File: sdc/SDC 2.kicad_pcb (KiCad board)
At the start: 2 copper layers, 70 x 56 mm, 122 parts, among them J1 BSPD_LED, J10 BMS_LED, J11 BSPD_Fault, J12 IMD_Fault, J13 BMS_Fault, J14 12V PWR, J15 SDC_IN, J16 SDC_OUT, J2 IMD_LED, J3 BMS_LED, J4 SW_Fault, J5 BSPD_BTN, J6 IMD_BTN, J7 BMS_BTN, J8 BSPD_LED, J9 IMD_LED, K1 G2RL-2A, K2 G2RL-2A, K3 G2RL-2A, K4 G2RL-2A, Q1 2N7002, Q2 2N7002, Q3 2N7002, Q4 2N7002, Q5 2N7002, Q6 2N7002, U1 VOM618AT, U10 AP2204K-ADJ, U2 VOM618AT, U3 TLV2371DBV, U4 TLV2371DBV, U6 VOM618AT, U7 VOM618AT, U8 TLV2371DBV, U9 AP2204K-ADJ

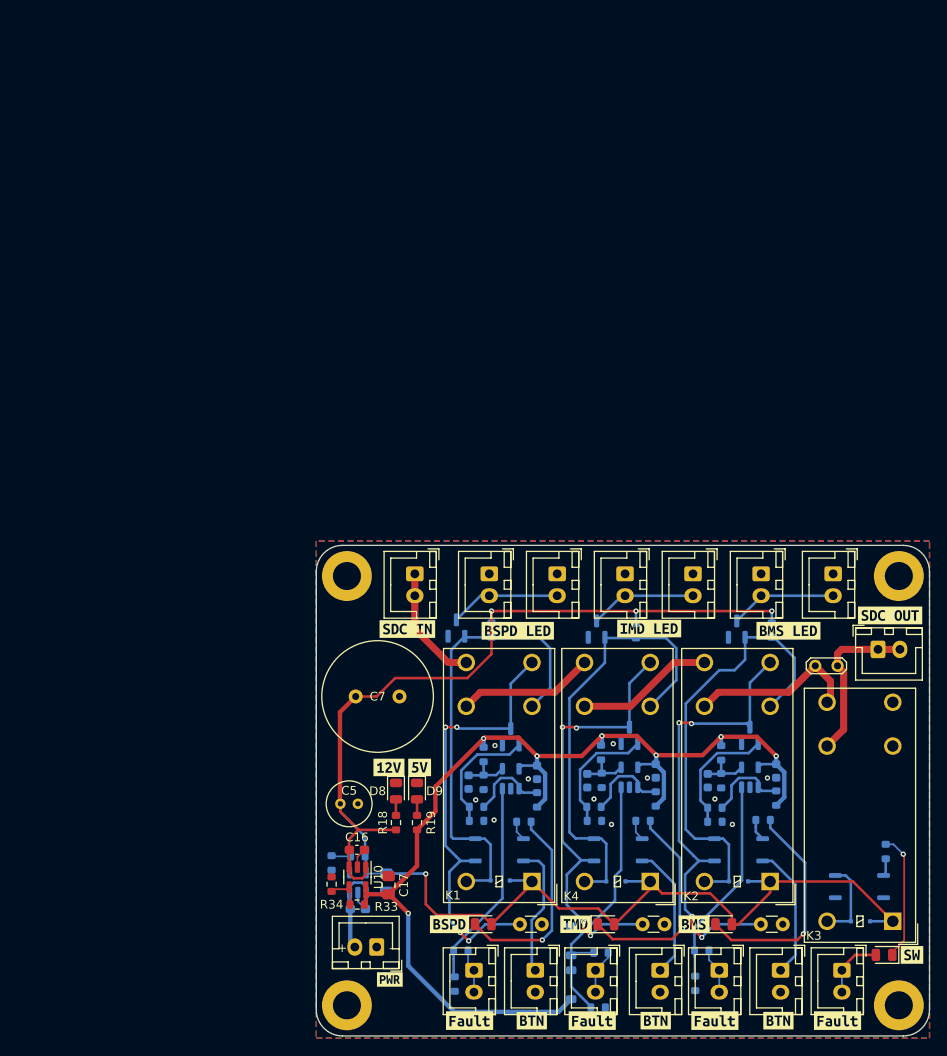
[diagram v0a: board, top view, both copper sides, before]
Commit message: Change JST to pin header
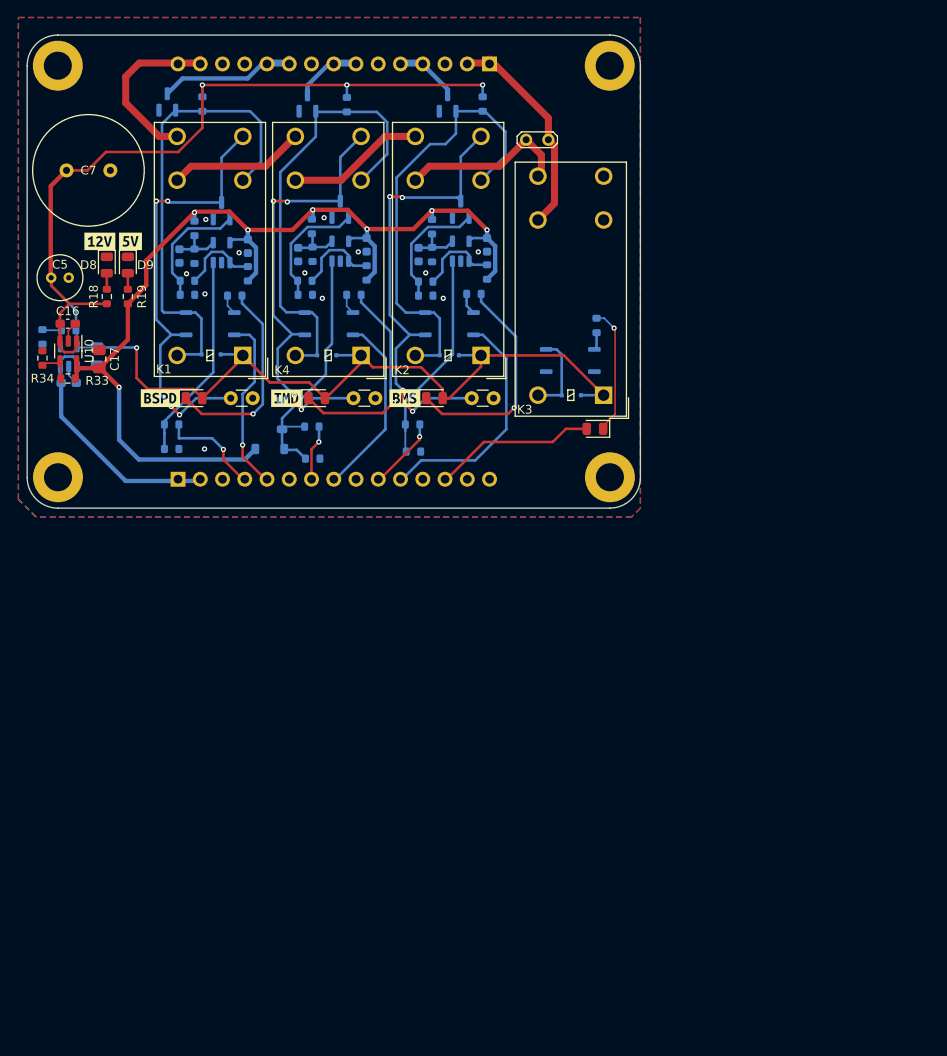
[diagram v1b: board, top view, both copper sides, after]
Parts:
- removed J1, J8: BSPD_LED, Connector_JST:JST_XH_B2B-XH-A_1x02_P2.50mm_Vertical
- removed J10, J3: BMS_LED, Connector_JST:JST_XH_B2B-XH-A_1x02_P2.50mm_Vertical
- removed J11: BSPD_Fault, Connector_JST:JST_XH_B2B-XH-A_1x02_P2.50mm_Vertical
- removed J12: IMD_Fault, Connector_JST:JST_XH_B2B-XH-A_1x02_P2.50mm_Vertical
- removed J13: BMS_Fault, Connector_JST:JST_XH_B2B-XH-A_1x02_P2.50mm_Vertical
- removed J14: 12V PWR, Connector_JST:JST_XH_B2B-XH-A_1x02_P2.50mm_Vertical
- removed J15: SDC_IN, Connector_JST:JST_XH_B2B-XH-A_1x02_P2.50mm_Vertical
- removed J16: SDC_OUT, Connector_JST:JST_XH_B2B-XH-A_1x02_P2.50mm_Vertical
- removed J2, J9: IMD_LED, Connector_JST:JST_XH_B2B-XH-A_1x02_P2.50mm_Vertical
- removed J4: SW_Fault, Connector_JST:JST_XH_B2B-XH-A_1x02_P2.50mm_Vertical
- removed J5: BSPD_BTN, Connector_JST:JST_XH_B2B-XH-A_1x02_P2.50mm_Vertical
- removed J6: IMD_BTN, Connector_JST:JST_XH_B2B-XH-A_1x02_P2.50mm_Vertical
- removed J7: BMS_BTN, Connector_JST:JST_XH_B2B-XH-A_1x02_P2.50mm_Vertical
- removed kibuzzard-67515B12: G***, kibuzzard-67515B12
- removed kibuzzard-67515B3D: G***, kibuzzard-67515B3D
- removed kibuzzard-67515B49: G***, kibuzzard-67515B49
- removed kibuzzard-67515B54: G***, kibuzzard-67515B54
- removed kibuzzard-67515B5C: G***, kibuzzard-67515B5C
- removed kibuzzard-67515BF5 (x3): G***, kibuzzard-67515BF5
- removed kibuzzard-67515BFB (x3): G***, kibuzzard-67515BFB
- removed kibuzzard-675169EE: G***, kibuzzard-675169EE
- removed kibuzzard-675169F2: G***, kibuzzard-675169F2
- removed kibuzzard-67A0C7EA: G***, kibuzzard-67A0C7EA
- added J17: Conn_01x15_Pin, Connector_PinHeader_2.54mm:PinHeader_1x15_P2.54mm_Vertical, B.Cu at (106.8, 49.3)
- added J18: Conn_01x15_Pin, Connector_PinHeader_2.54mm:PinHeader_1x15_P2.54mm_Vertical, B.Cu at (71.2, 96.7)
- moved R22 70.6 mm to (86.6, 94.3)
- moved D6 70.2 mm to (81.7, 93.2), turned to 0 degrees
- moved R5 69.1 mm to (70.5, 93.2), turned to 0 degrees
- moved H2 68.7 mm to (57.5, 96.5)
- moved H4 68.7 mm to (120.5, 96.5)
- moved R6 68.7 mm to (98.1, 93.5), turned to 0 degrees
- moved R11 68.5 mm to (79.2, 73.2)
- moved R3 68.5 mm to (77.7, 75.8)
- moved R34 68.5 mm to (55.7, 82.9)
- moved U10 68.5 mm to (58.7, 82.1)
- moved C1 68.5 mm to (71.4, 71.2)
- moved C10 68.5 mm to (79.2, 70.1)
- moved C11 68.5 mm to (91.2, 87.5)
- moved C12 68.5 mm to (77.2, 87.5)
- moved C13 68.5 mm to (104.7, 87.5)
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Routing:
- net VDC: track 10.1 -> 28.3 mm
- net SW_Fault: track 6.18 -> 18.3 mm
- net BMS_RST: track 15.4 -> 27.5 mm
- net BSPD_FAULT: track 4.53 -> 11.8 mm, vias 0 -> 1
- net BSPD_IN: track 13.3 -> 19.8 mm
- net SW_OUT: track 18.5 -> 24.8 mm
- net IMD_RST: track 15.4 -> 21.3 mm
- net BSPD_RST: track 15.2 -> 20.4 mm, vias 0 -> 1
- net BMS_LED: track 12.2 -> 7.19 mm
- net IMD_LED: track 12.4 -> 7.85 mm
- net +5V: track 125.0 -> 120.6 mm
- net BSPD_LED: track 12.6 -> 16.5 mm
- net BMS_FAULT: track 4.74 -> 8.41 mm, vias 0 -> 1
- net IMD_FAULT: track 4.60 -> 6.56 mm, vias 0 -> 1
- net Net-(D6-A): track 31.6 -> 29.7 mm
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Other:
- board size 70 x 56 mm -> 70 x 54 mm
- board text removed: "+ -"

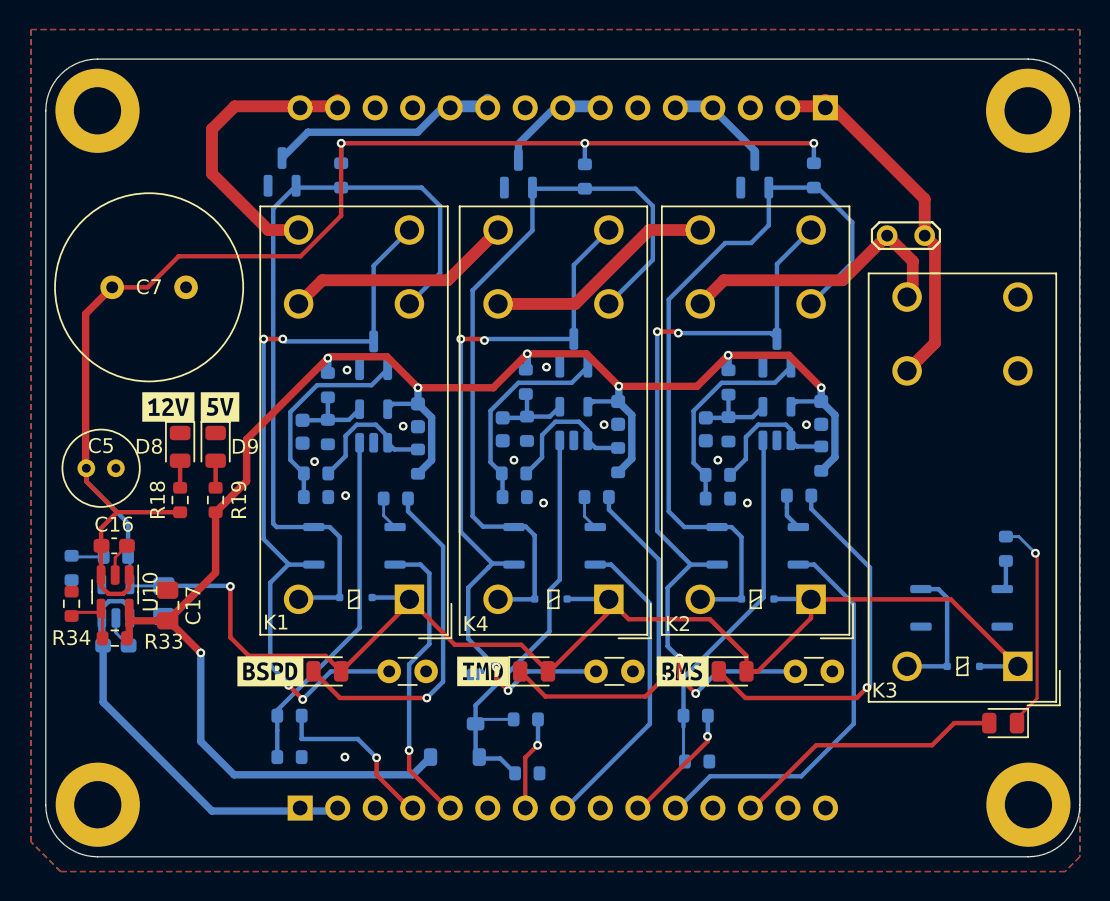
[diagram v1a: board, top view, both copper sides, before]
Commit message: feat: use 2x10 pin
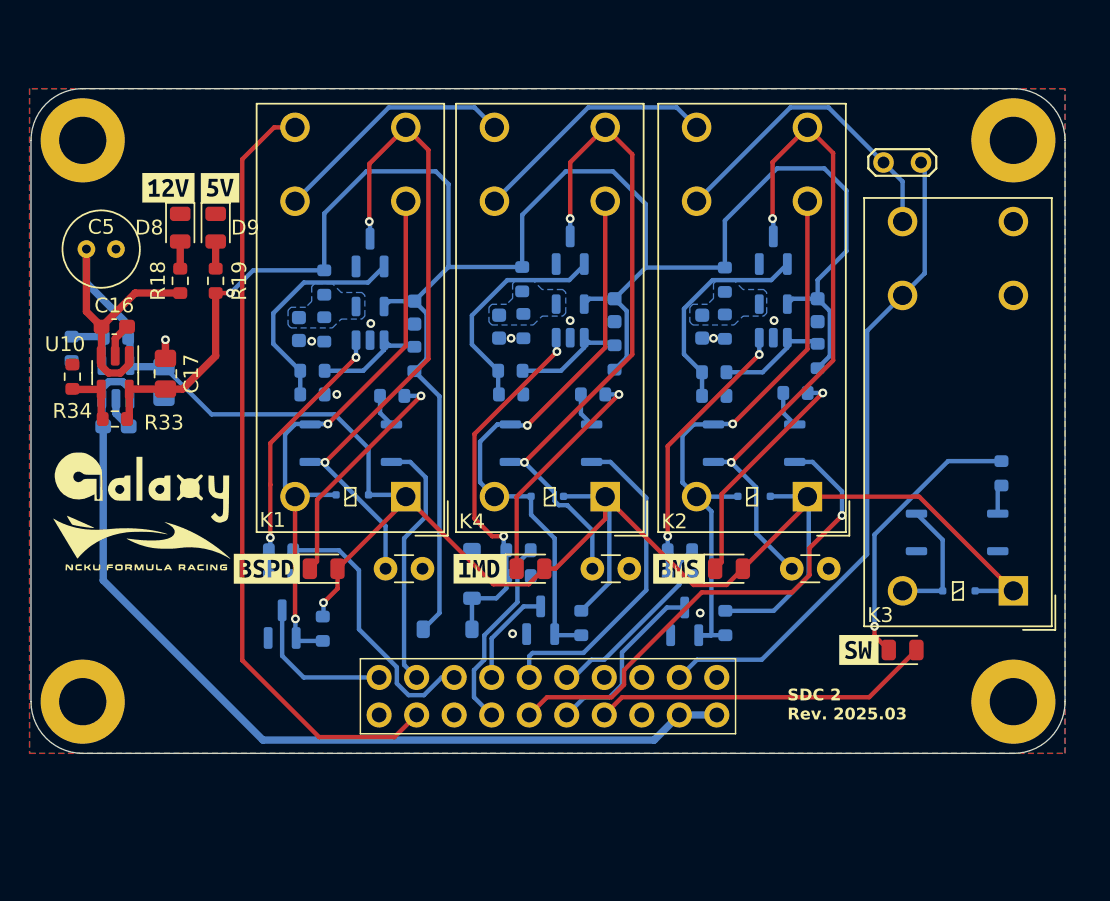
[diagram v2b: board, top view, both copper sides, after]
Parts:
- removed C7: 220u, Capacitor_THT:C_Radial_D12.5mm_H25.0mm_P5.00mm
- removed J17, J18: Conn_01x15_Pin, Connector_PinHeader_2.54mm:PinHeader_1x15_P2.54mm_Vertical
- added J1: Conn_02x10_Odd_Even, Connector_PinHeader_2.54mm:PinHeader_2x10_P2.54mm_Vertical, F.Cu at (99.4, 87.9)
- added kibuzzard-67D10362: G***, kibuzzard-67D10362, F.Cu at (109.0, 86.0)
- G*** (x2): moved to F.Cu
- moved H4 64.4 mm to (56.5, 89.5)
- moved H2 62.4 mm to (119.5, 89.5)
- moved R29 30.9 mm to (100.0, 84.2)
- moved R25 30.7 mm to (72.8, 84.6)
- moved Q5 30.7 mm to (97.2, 84.1)
- moved Q3 30.6 mm to (70.0, 84.2)
- moved Q6 30.3 mm to (87.5, 84.0)
- moved R30 30.2 mm to (90.2, 84.2)
- moved G*** 16.8 mm to (60.5, 75.0), turned to 0 degrees
- moved C17 15.7 mm to (62.1, 67.3)
- moved R34 15.4 mm to (55.8, 67.5)
- moved C14 14.8 mm to (58.8, 70.9)
- moved C15 14.8 mm to (62.0, 67.9)
- moved C16 14.8 mm to (58.6, 64.1)
- moved C5 14.8 mm to (56.8, 58.9)
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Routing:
- net +12V: track 186.0 -> 144.6 mm, vias 4 -> 1
- net VDC: track 28.3 -> 62.7 mm
- net BSPD_IN: track 19.8 -> 53.0 mm
- net SW_OUT: track 24.8 -> 44.4 mm
- net +5V: track 120.6 -> 138.6 mm, vias 7 -> 1
- net BSPD_FAULT_OUT: track 52.9 -> 40.5 mm, vias 0 -> 2
- net IMD_FAULT_OUT: track 51.9 -> 39.5 mm, vias 0 -> 1
- net BMS_FAULT_OUT: track 51.7 -> 40.7 mm, vias 0 -> 1
- net Net-(D2-K): track 25.8 -> 15.9 mm
- net Net-(D10-K): track 24.7 -> 15.6 mm
- net Net-(Q2-D): track 52.2 -> 44.8 mm, vias 4 -> 2
- net Net-(D1-K): track 23.4 -> 15.9 mm
- net IMD_FAULT: track 6.56 -> 13.2 mm, vias 1 -> 0
- net BSPD_FAULT: track 11.8 -> 18.4 mm, vias 1 -> 0
- net BMS_RST: track 27.5 -> 34.1 mm, vias 0 -> 1
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- added copper zone on B.Cu, net Net-(U3--)
- added copper zone on B.Cu, net Net-(U4--)
- added copper zone on B.Cu, net Net-(U8--)
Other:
- board size 70 x 54 mm -> 70 x 45 mm
- board text added: "SDC 2 Rev. 2025.03"

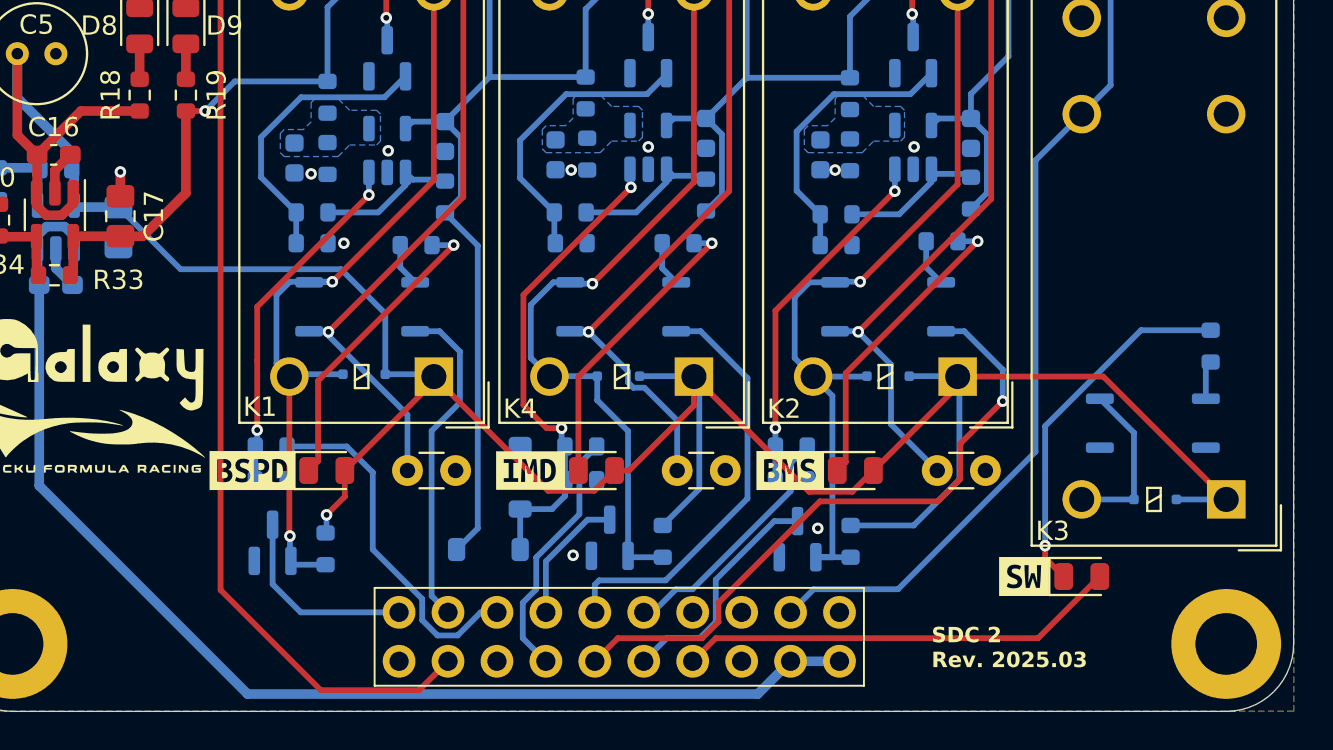
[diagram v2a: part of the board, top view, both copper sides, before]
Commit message: chore: remove pull up resistor and change flyback diodes
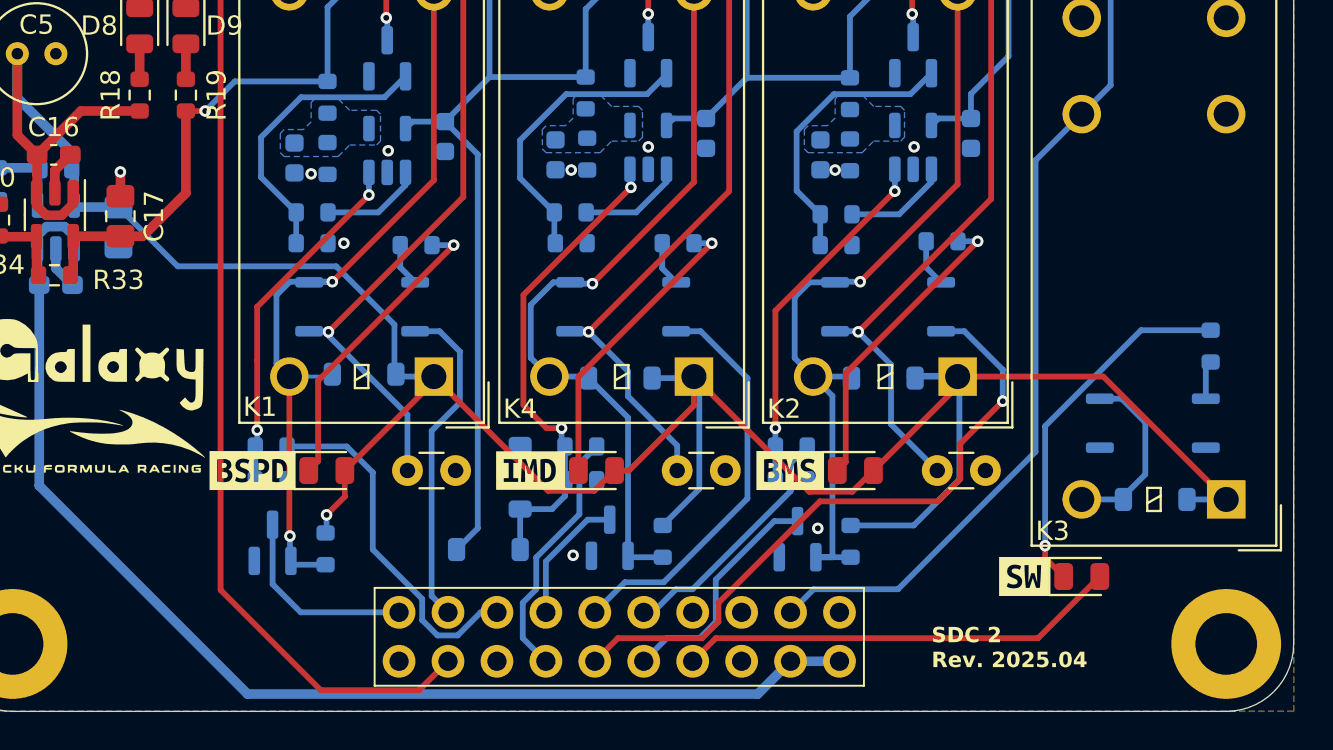
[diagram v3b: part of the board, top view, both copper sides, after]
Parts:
- removed R11, R12, R26: 1k, Resistor_SMD:R_0603_1608Metric
- D11, D12, D3, D4: value 1SS355VM -> 1N4148W; footprint Diode_SMD:D_SOD-323F -> Diode_SMD:D_SOD-123
- R20: value 100R -> 10k
- moved D4 13.9 mm to (88.0, 75.7)
- moved D12 13.8 mm to (101.7, 75.7)
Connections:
- D12 pad 2: IMD_FAULT_OUT -> BMS_FAULT_OUT
- D4 pad 2: BMS_FAULT_OUT -> IMD_FAULT_OUT
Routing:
- net +5V: track 138.6 -> 127.0 mm
- net Net-(R27-Pad1): track 7.75 -> 5.49 mm
- net Net-(R13-Pad1): track 7.51 -> 5.27 mm
- net Net-(R14-Pad1): track 7.70 -> 5.48 mm
- net IMD_RST: track 22.2 -> 21.3 mm
- net Net-(D11-A): track 8.68 -> 9.50 mm
- net BMS_FAULT_OUT: track 40.7 -> 39.9 mm
- net +12V: track 144.6 -> 145.3 mm
- net BSPD_FAULT_OUT: track 40.5 -> 39.9 mm
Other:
- board text added: "SDC 2 Rev. 2025.04"
- board text removed: "SDC 2 Rev. 2025.03"
